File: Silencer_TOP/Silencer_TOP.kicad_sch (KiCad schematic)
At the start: 35 parts, among them T100 2N3904, T101 2N3904, T102 2N3904, T103 2N3904

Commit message: Top board initial placement.
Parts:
- JP1, JP100: footprint (none) -> AO_tht:PinHeader_1x08_P2.54mm_Vertical
- R100, R101, R102, R103, R104, R105, R106, R107, R108, R109, R110, R111, R112: footprint (none) -> AO_tht:R_Axial_DIN0207_L6.3mm_D2.5mm_P10.16mm_Horizontal
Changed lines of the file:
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@@
 (kicad_sch
-	(version 20231120)
+	(version 20250114)
 	(generator "eeschema")
-	(generator_version "8.0")
+	(generator_version "9.0")
 	(paper "A4")
 	(junction
@@
 			)
 		)
-		(property "Footprint" ""
+		(property "Footprint" "AO_tht:R_Axial_DIN0207_L6.3mm_D2.5mm_P10.16mm_Horizontal"
 			(at 49.53 151.638 90)
 			(effects
@@
 			)
 		)
-		(property "Footprint" ""
+		(property "Footprint" "AO_tht:PinHeader_1x08_P2.54mm_Vertical"
 			(at 143.51 39.37 0)
 			(effects
@@
 			)
 		)
-		(property "Footprint" ""
+		(property "Footprint" "AO_tht:R_Axial_DIN0207_L6.3mm_D2.5mm_P10.16mm_Horizontal"
 			(at 232.41 44.958 90)
 			(effects
@@
 			)
 		)
-		(property "Footprint" ""
+		(property "Footprint" "AO_tht:R_Axial_DIN0207_L6.3mm_D2.5mm_P10.16mm_Horizontal"
 			(at 100.33 89.408 90)
 			(effects
@@
 			)
 		)
-		(property "Footprint" ""
+		(property "Footprint" "AO_tht:R_Axial_DIN0207_L6.3mm_D2.5mm_P10.16mm_Horizontal"
 			(at 179.07 89.408 90)
 			(effects
@@
 			)
 		)
-		(property "Footprint" ""
+		(property "Footprint" "AO_tht:R_Axial_DIN0207_L6.3mm_D2.5mm_P10.16mm_Horizontal"
 			(at 71.12 99.568 90)
 			(effects
@@
 			)
 		)
-		(property "Footprint" ""
+		(property "Footprint" "AO_tht:R_Axial_DIN0207_L6.3mm_D2.5mm_P10.16mm_Horizontal"
 			(at 100.33 131.318 90)
 			(effects
@@
 			)
 		)
-		(property "Footprint" ""
+		(property "Footprint" "AO_tht:R_Axial_DIN0207_L6.3mm_D2.5mm_P10.16mm_Horizontal"
 			(at 128.27 109.728 90)
 			(effects
@@
 			)
 		)
-		(property "Footprint" ""
+		(property "Footprint" "AO_tht:R_Axial_DIN0207_L6.3mm_D2.5mm_P10.16mm_Horizontal"
 			(at 149.86 99.568 90)
 			(effects
@@
 			)
 		)
-		(property "Footprint" ""
+		(property "Footprint" "AO_tht:R_Axial_DIN0207_L6.3mm_D2.5mm_P10.16mm_Horizontal"
 			(at 71.12 141.478 90)
 			(effects
@@
 			)
 		)
-		(property "Footprint" ""
+		(property "Footprint" "AO_tht:R_Axial_DIN0207_L6.3mm_D2.5mm_P10.16mm_Horizontal"
 			(at 128.27 151.638 90)
 			(effects
@@
 			)
 		)
-		(property "Footprint" ""
+		(property "Footprint" "AO_tht:R_Axial_DIN0207_L6.3mm_D2.5mm_P10.16mm_Horizontal"
 			(at 149.86 141.478 90)
 			(effects
@@
 			)
 		)
-		(property "Footprint" ""
+		(property "Footprint" "AO_tht:R_Axial_DIN0207_L6.3mm_D2.5mm_P10.16mm_Horizontal"
 			(at 179.07 131.318 90)
 			(effects
@@
 			)
 		)
-		(property "Footprint" ""
+		(property "Footprint" "AO_tht:PinHeader_1x08_P2.54mm_Vertical"
 			(at 177.8 39.37 0)
 			(effects
@@
 			)
 		)
-		(property "Footprint" ""
+		(property "Footprint" "AO_tht:R_Axial_DIN0207_L6.3mm_D2.5mm_P10.16mm_Horizontal"
 			(at 49.53 109.728 90)
 			(effects
@@
 		)
 	)
+	(embedded_fonts no)
 )

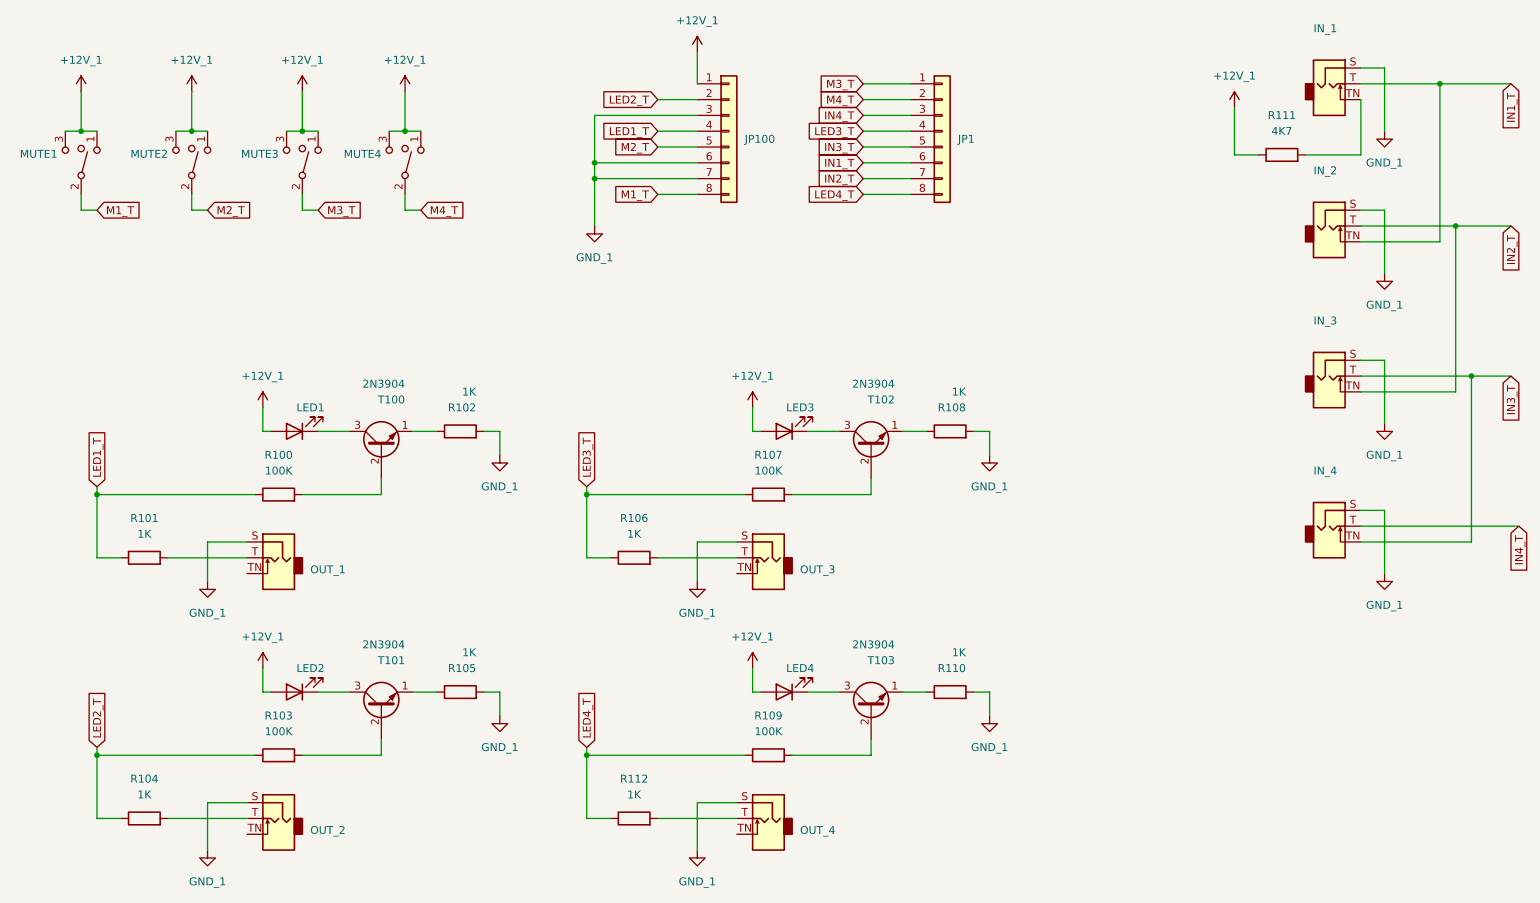
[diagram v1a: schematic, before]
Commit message: Refactor Top and Bottom Schematics.
Had to move input/output jacks to bottom board.  This required a full refactoring of both and will mean re-doing the pcb layout of the top board.
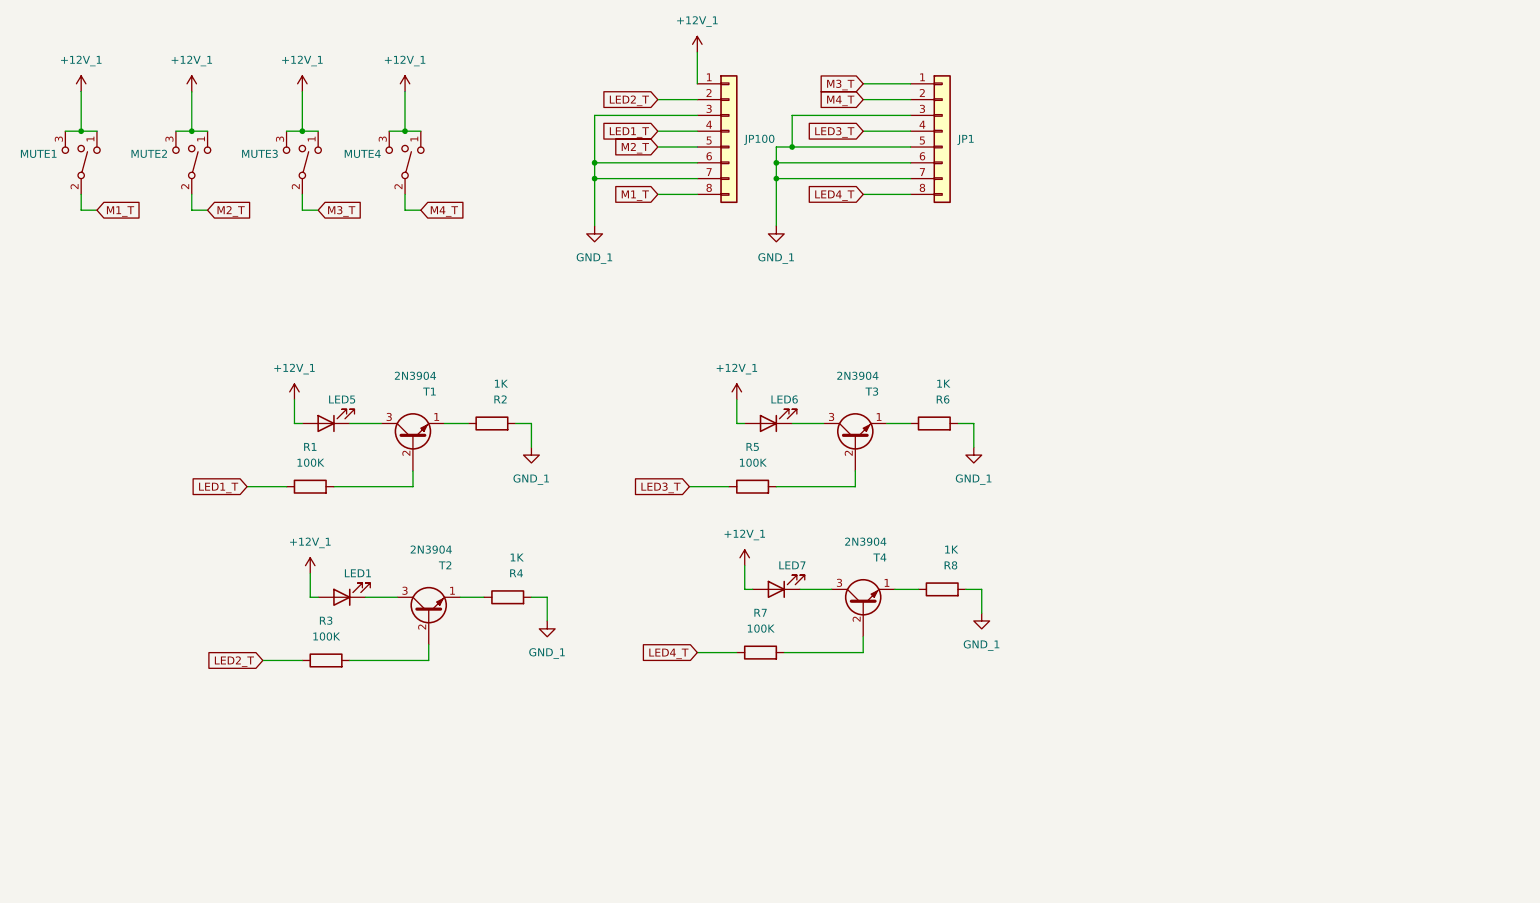
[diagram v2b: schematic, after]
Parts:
- removed IN_1, IN_2, IN_3, IN_4, OUT_1, OUT_2, OUT_3, OUT_4: AudioJack2_SwitchT, AO_tht:Jack_6.35mm_PJ_629HAN_slots, symbol AO_symbols:AudioJack2_SwitchT
- removed LED2, LED3, LED4: LED_red, AO_tht:LED_D5.0mm, symbol AO_symbols:LED_red
- removed R100, R103, R107, R109: 100K, AO_tht:R_Axial_DIN0207_L6.3mm_D2.5mm_P10.16mm_Horizontal, symbol Device:R
- removed R101, R102, R104, R105, R106, R108, R110, R112: 1K, AO_tht:R_Axial_DIN0207_L6.3mm_D2.5mm_P10.16mm_Horizontal, symbol Device:R
- removed R111: 4K7, AO_tht:R_Axial_DIN0207_L6.3mm_D2.5mm_P10.16mm_Horizontal, symbol Device:R
- removed T100, T101, T102, T103: 2N3904, AO_tht:TO-92_Inline_Wide, symbol AO_symbols:2N3904
- added LED5, LED6, LED7: LED_red, AO_tht:LED_D5.0mm, symbol AO_symbols:LED_red
- added R1, R3, R5, R7: 100K, AO_tht:R_Axial_DIN0207_L6.3mm_D2.5mm_P10.16mm_Horizontal, symbol Device:R
- added R2, R4, R6, R8: 1K, AO_tht:R_Axial_DIN0207_L6.3mm_D2.5mm_P10.16mm_Horizontal, symbol Device:R
- added T1, T2, T3, T4: 2N3904, AO_tht:TO-92_Inline_Wide, symbol AO_symbols:2N3904
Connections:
- net IN1_T is gone; now on net GND_1: JP1.6 (Pin_6)
- net IN2_T is gone; now on net GND_1: JP1.7 (Pin_7)
- net IN3_T is gone; now on net GND_1: JP1.5 (Pin_5)
- net IN4_T is gone; now on net GND_1: JP1.3 (Pin_3)
- net +12V_1: now also LED5.2 (A), LED6.2 (A), LED7.2 (A)
- net GND_1: now also R2.2, R4.2, R6.2, R8.2
- net LED1_T: now also R1.1
- net LED2_T: now also R3.1
- net LED3_T: now also R5.1
- net LED4_T: now also R7.1
- net at LED1.1 (K): now also T2.3 (C)
- new net: R6.1, T3.1 (E)
- new net: R5.2, T3.2 (B)
- new net: LED6.1 (K), T3.3 (C)
- new net: R2.1, T1.1 (E)
- new net: R1.2, T1.2 (B)
- new net: LED5.1 (K), T1.3 (C)
- new net: R8.1, T4.1 (E)
- new net: R7.2, T4.2 (B)
- new net: LED7.1 (K), T4.3 (C)
- new net: R4.1, T2.1 (E)
- new net: R3.2, T2.2 (B)

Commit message: Bottom board layout roughed out.  Routing began
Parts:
- renumbered JP100 to JP2
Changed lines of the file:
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@@
 		(dnp no)
 		(fields_autoplaced yes)
-		(property "Reference" "JP100"
+		(property "Reference" "JP2"
 			(at 146.05 40.6399 0)
 			(effects
@@
 			(project ""
 				(path "/451cde18-0dd5-48df-b1b1-576c1ce7d90e"
-					(reference "JP100")
+					(reference "JP2")
 					(unit 1)
 				)
